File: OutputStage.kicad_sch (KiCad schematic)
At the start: 11 parts, among them SW63 SW_Rotary_1x7_MP, SW64 SW_SPDT, SW69 SW_SPDT, U10 BUF634A

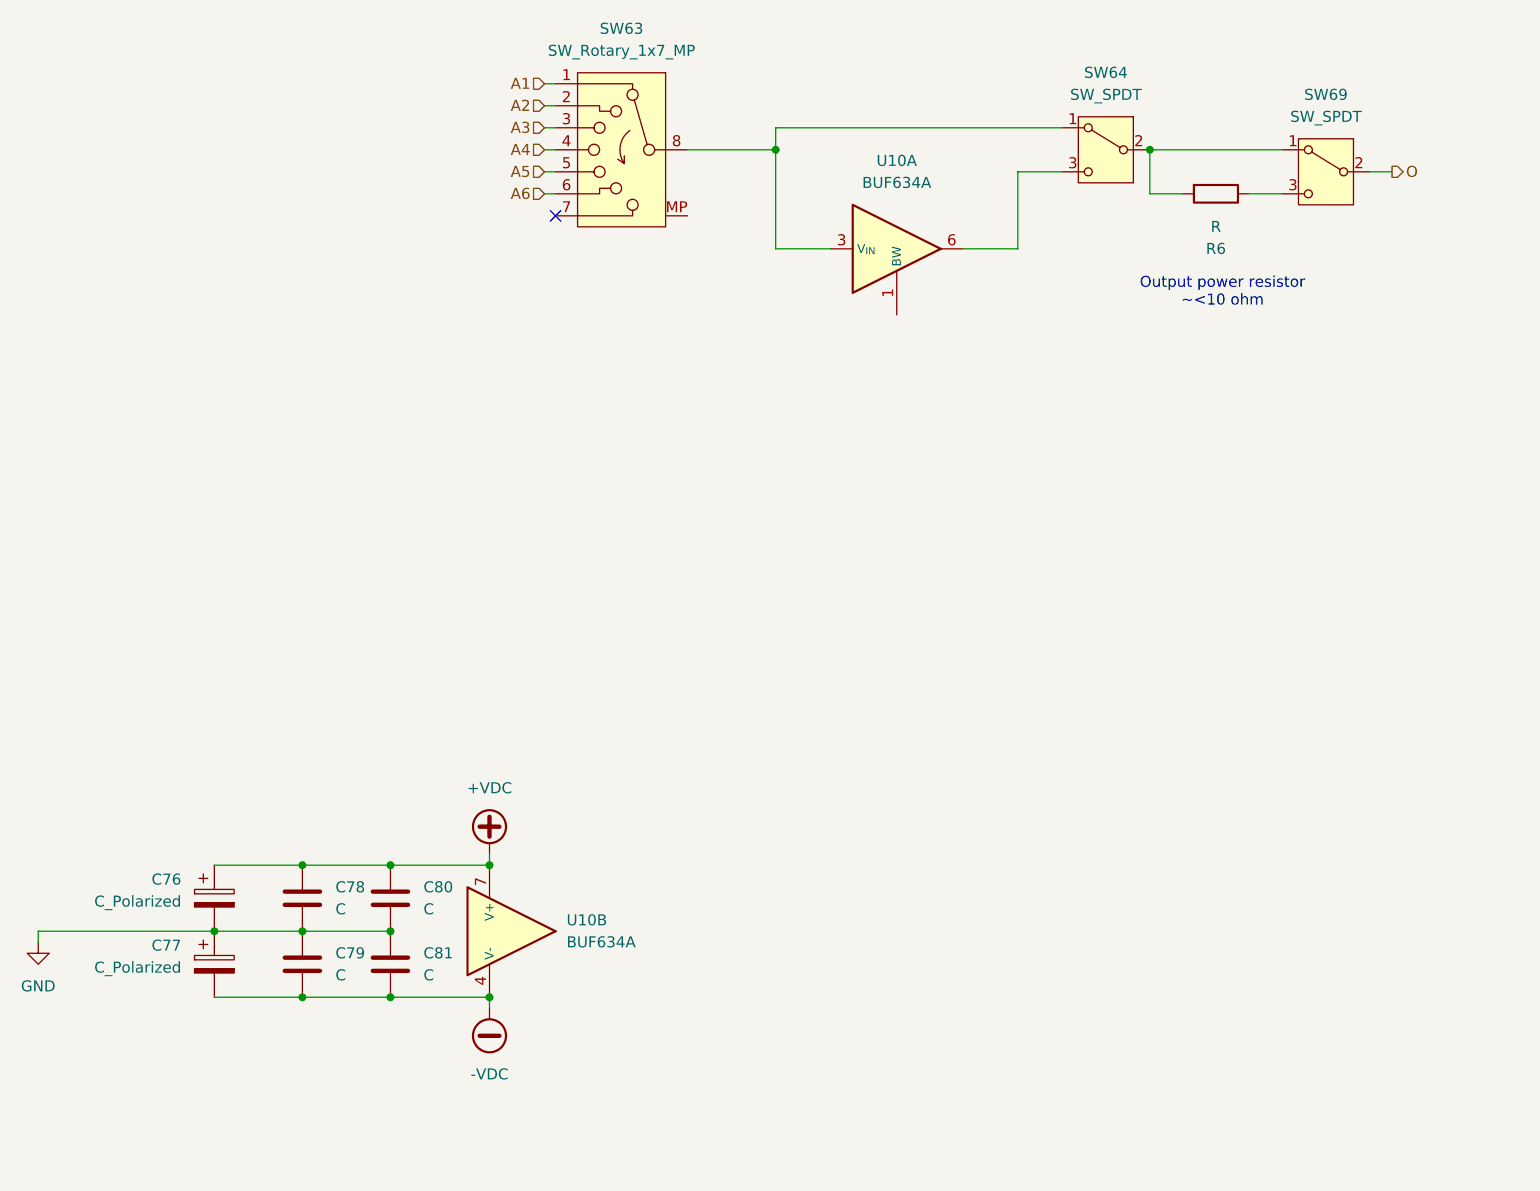
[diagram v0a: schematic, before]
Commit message: minor schematic changes, 4 way dip now used instead of 6. switch and pot footprints and symbols done
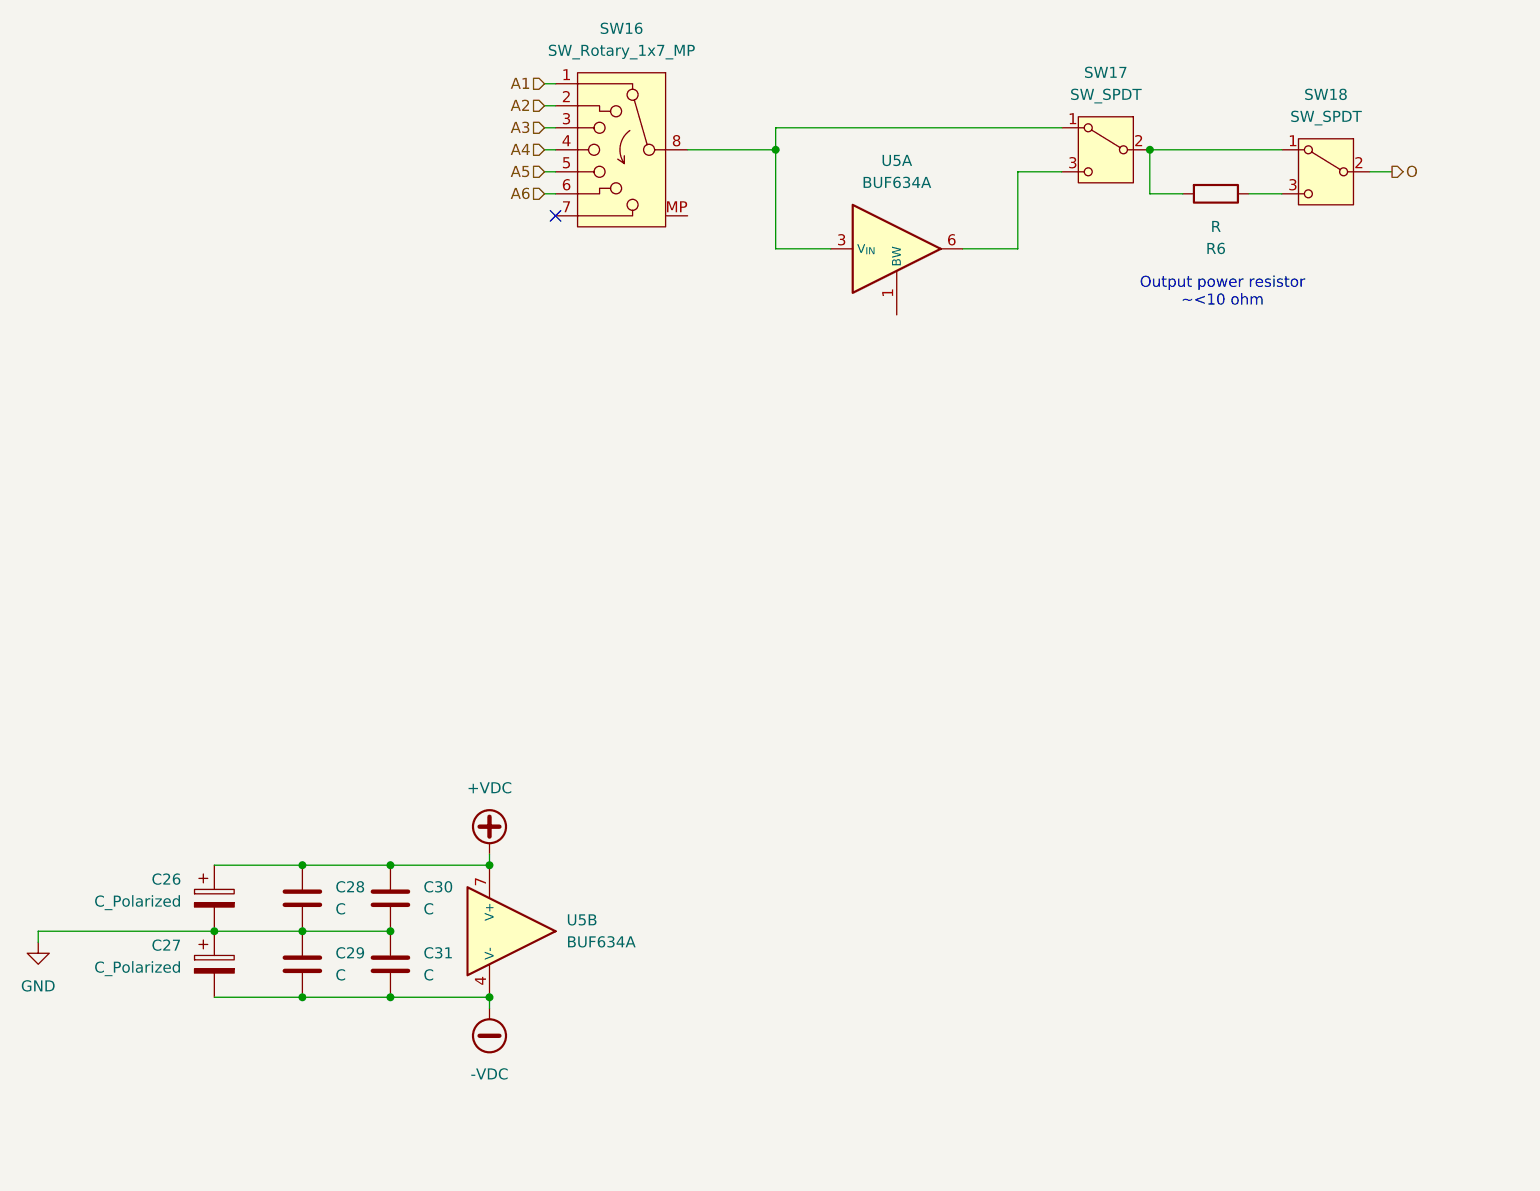
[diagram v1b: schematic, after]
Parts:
- renumbered C76 to C26, C77 to C27, C78 to C28, C79 to C29, C80 to C30, C81 to C31, SW63 to SW16, SW64 to SW17, SW69 to SW18, U10 to U5

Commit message: Initial PCB layout
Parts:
- renumbered C26 to C25, C27 to C26, C28 to C27, C29 to C28, C30 to C29, C31 to C30, SW16 to SW11, SW17 to SW12, SW18 to SW13
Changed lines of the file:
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@@
 		(dnp no)
 		(fields_autoplaced yes)
-		(property "Reference" "C28"
+		(property "Reference" "C27"
 			(at 60.96 161.2899 0)
 			(show_name no)
@@
 			(project "universalOpAmpV0"
 				(path "/0c9d5097-e341-4aa8-a29f-4bc5e653f52f/ce779b8f-d582-4e38-8190-accd009e9506"
-					(reference "C28")
+					(reference "C27")
 					(unit 1)
 				)
@@
 		(in_pos_files yes)
 		(dnp no)
-		(property "Reference" "C26"
+		(property "Reference" "C25"
 			(at 43.18 160.4009 0)
 			(show_name no)
@@
 			(project "universalOpAmpV0"
 				(path "/0c9d5097-e341-4aa8-a29f-4bc5e653f52f/ce779b8f-d582-4e38-8190-accd009e9506"
-					(reference "C26")
+					(reference "C25")
 					(unit 1)
 				)
@@
 		(in_pos_files yes)
 		(dnp no)
-		(property "Reference" "C27"
+		(property "Reference" "C26"
 			(at 43.18 168.0209 0)
 			(show_name no)
@@
 			(project "universalOpAmpV0"
 				(path "/0c9d5097-e341-4aa8-a29f-4bc5e653f52f/ce779b8f-d582-4e38-8190-accd009e9506"
-					(reference "C27")
+					(reference "C26")
 					(unit 1)
 				)
@@
 		(dnp no)
 		(fields_autoplaced yes)
-		(property "Reference" "C29"
+		(property "Reference" "C28"
 			(at 60.96 168.9099 0)
 			(show_name no)
@@
 			(project "universalOpAmpV0"
 				(path "/0c9d5097-e341-4aa8-a29f-4bc5e653f52f/ce779b8f-d582-4e38-8190-accd009e9506"
-					(reference "C29")
+					(reference "C28")
 					(unit 1)
 				)
@@
 		(dnp no)
 		(fields_autoplaced yes)
-		(property "Reference" "C31"
+		(property "Reference" "C30"
 			(at 71.12 168.9099 0)
 			(show_name no)
@@
 			(project "universalOpAmpV0"
 				(path "/0c9d5097-e341-4aa8-a29f-4bc5e653f52f/ce779b8f-d582-4e38-8190-accd009e9506"
-					(reference "C31")
+					(reference "C30")
 					(unit 1)
 				)
@@
 		(dnp no)
 		(fields_autoplaced yes)
-		(property "Reference" "C30"
+		(property "Reference" "C29"
 			(at 71.12 161.2899 0)
 			(show_name no)
@@
 			(project "universalOpAmpV0"
 				(path "/0c9d5097-e341-4aa8-a29f-4bc5e653f52f/ce779b8f-d582-4e38-8190-accd009e9506"
-					(reference "C30")
+					(reference "C29")
 					(unit 1)
 				)
@@
 		(dnp no)
 		(fields_autoplaced yes)
-		(property "Reference" "SW18"
+		(property "Reference" "SW13"
 			(at 175.26 69.85 0)
 			(show_name no)
@@
 			(project "universalOpAmpV0"
 				(path "/0c9d5097-e341-4aa8-a29f-4bc5e653f52f/ce779b8f-d582-4e38-8190-accd009e9506"
-					(reference "SW18")
+					(reference "SW13")
 					(unit 1)
 				)
@@
 		(dnp no)
 		(fields_autoplaced yes)
-		(property "Reference" "SW17"
+		(property "Reference" "SW12"
 			(at 149.86 67.31 0)
 			(show_name no)
@@
 			(project "universalOpAmpV0"
 				(path "/0c9d5097-e341-4aa8-a29f-4bc5e653f52f/ce779b8f-d582-4e38-8190-accd009e9506"
-					(reference "SW17")
+					(reference "SW12")
 					(unit 1)
 				)
@@
 		(dnp no)
 		(fields_autoplaced yes)
-		(property "Reference" "SW16"
+		(property "Reference" "SW11"
 			(at 93.98 62.23 0)
 			(show_name no)
@@
 			(project "universalOpAmpV0"
 				(path "/0c9d5097-e341-4aa8-a29f-4bc5e653f52f/ce779b8f-d582-4e38-8190-accd009e9506"
-					(reference "SW16")
-					(unit 1)
-				)
+					(reference "SW11")
+					(unit 1)
+				)

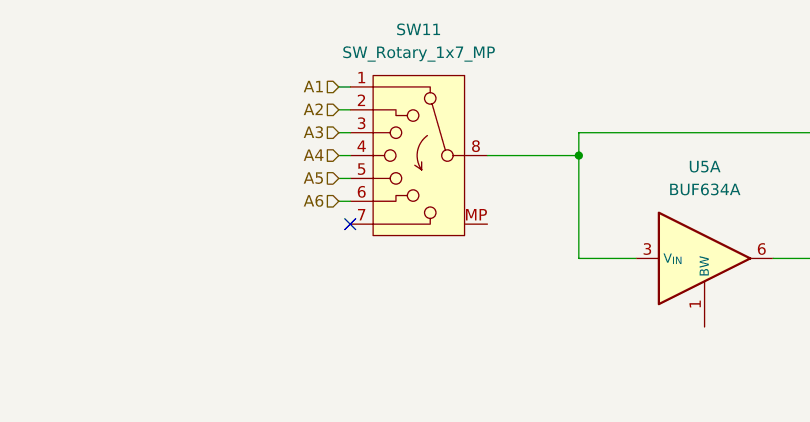
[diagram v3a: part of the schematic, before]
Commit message: input stage schematic done, layout WIP
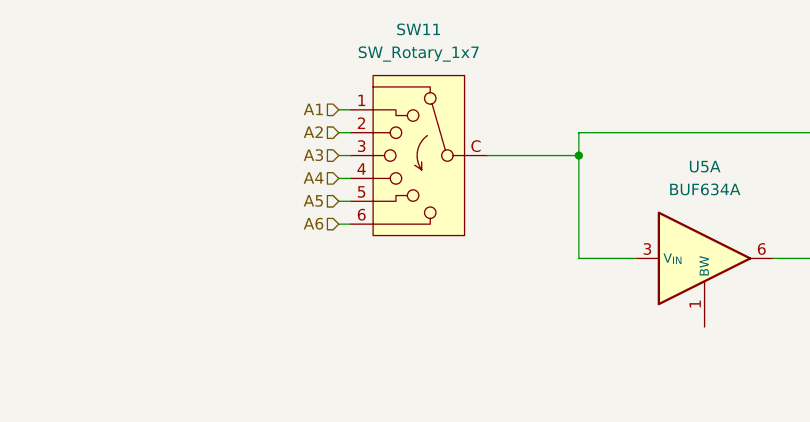
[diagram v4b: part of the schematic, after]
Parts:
- removed SW11: SW_Rotary_1x7_MP, symbol Switch:SW_Rotary_1x7_MP
- added SW11: SW_Rotary_1x7, uniOpAmpLib:SS-10-16, symbol uniOpAmpLib:SW_Rotary_1x7
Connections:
- net A1: now also SW11.1
- net A2: now also SW11.2
- net A3: now also SW11.3
- net A4: now also SW11.4
- net A5: now also SW11.5
- net A6: now also SW11.6
- net at SW12.1 (A), U5.3 (V_{IN}): now also SW11.C
- no-connect marks 1 -> 0

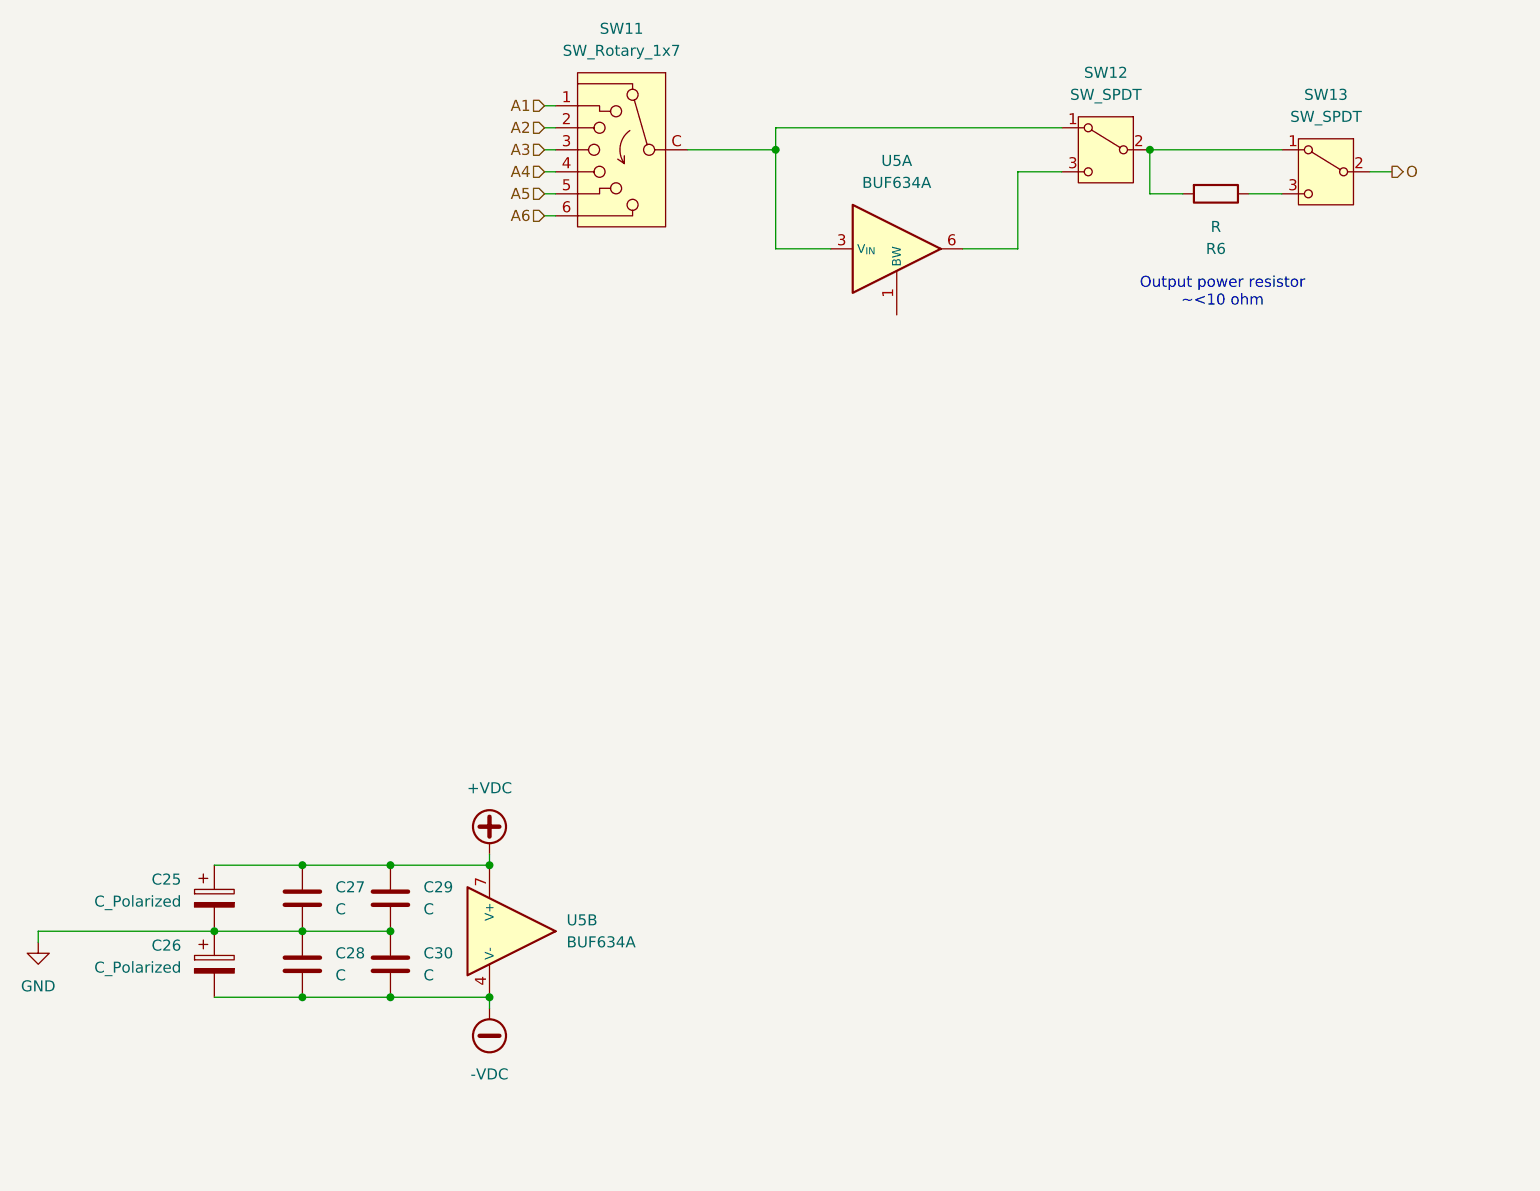
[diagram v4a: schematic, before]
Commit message: Input and output routing complete
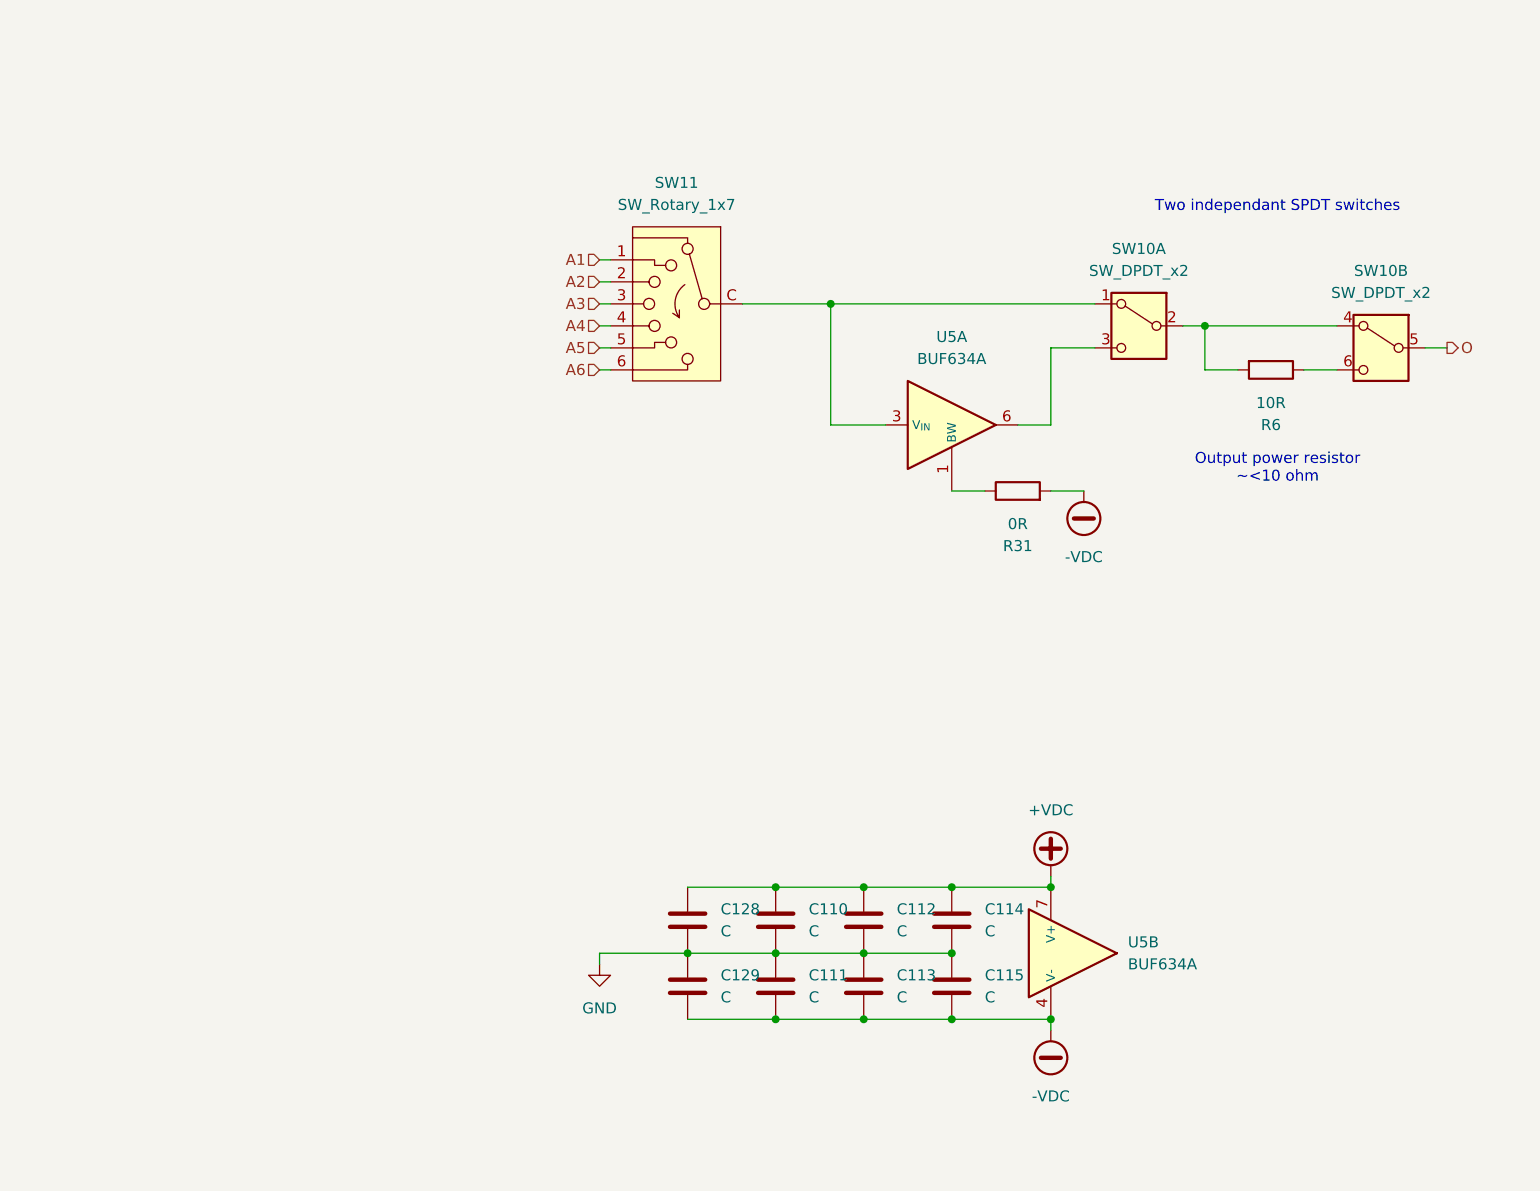
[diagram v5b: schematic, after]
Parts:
- removed C25, C26: C_Polarized, symbol Device:C_Polarized
- removed C27, C28, C29, C30: C, symbol Device:C
- removed SW12, SW13: SW_SPDT, symbol Switch:SW_SPDT
- added C110, C111, C112, C113, C114, C115, C128, C129: C, uniOpAmpLib:C_0805_Metric2012_HandSolder, symbol Device:C
- added R31: 0R, Resistor_SMD:R_0805_2012Metric_Pad1.20x1.40mm_HandSolder, symbol Device:R
- added SW10: SW_DPDT_x2, uniOpAmpLib:CAS-DxxB, symbol Switch:SW_DPDT_x2
- R6: value R -> 10R; footprint (none) -> Resistor_SMD:R_2512_6332Metric_Pad1.40x3.35mm_HandSolder
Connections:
- net +VDC: now also C110.1, C112.1, C114.1, C128.1
- net -VDC: now also C111.2, C113.2, C115.2, C129.2, R31.2
- net GND: now also C110.2, C111.1, C112.2, C113.1, C114.2, C115.1, C128.2, C129.1
- net O: now also SW10.5 (B)
- net at SW11.C, U5.3 (V_{IN}): now also SW10.1 (A)
- net at R6.2: now also SW10.2 (B), SW10.4 (A)
- net at R6.1: now also SW10.6 (C)
- net at U5.6: now also SW10.3 (C)
- net at U5.1 (BW): now also R31.1
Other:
- note added: "Two independant SPDT switches"
- moved on the sheet: R6, SW11, U5A, U5B
